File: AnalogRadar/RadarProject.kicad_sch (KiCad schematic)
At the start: 68 parts, among them J1 Conn_Coaxial, J2 Conn_Coaxial, J3 Conn_01x05, Q1 Q_NPN_BCE, SW1 SW_SPDT, U1 AT0603T03ECATD, U2 PD2328J5050S2HF, U3 BGU8052, U4 BGU8052, U5 CVCO55CC-2230-2430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

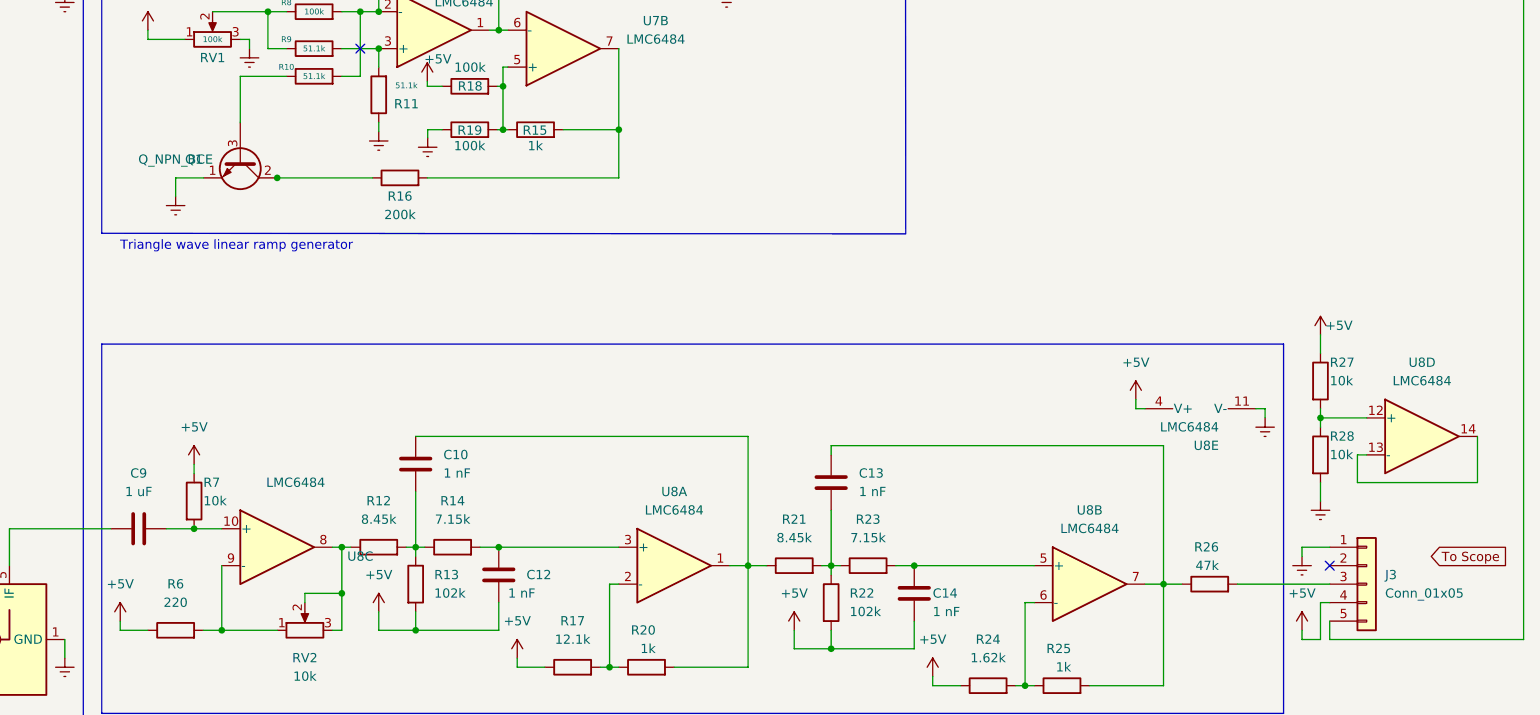
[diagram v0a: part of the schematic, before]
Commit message: added pico carrier board
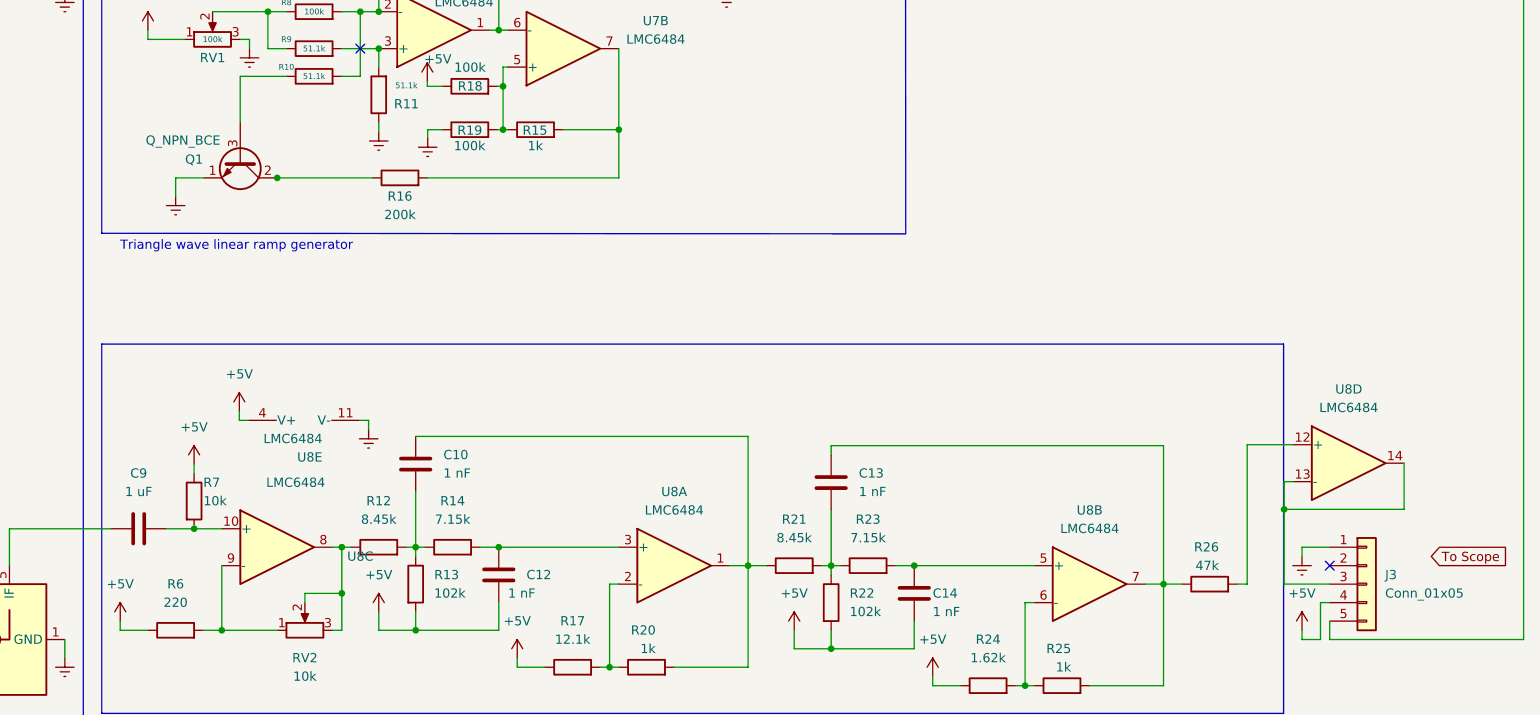
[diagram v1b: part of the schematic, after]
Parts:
- removed R27, R28: 10k, Resistor_SMD:R_0805_2012Metric, symbol Device:R
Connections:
- net at U8.12 (+): now also R26.2
- net at U8.13 (-), U8.14: now also J3.3 (Pin_3)
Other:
- moved on the sheet: U8D, U8E
